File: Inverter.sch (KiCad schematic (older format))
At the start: 96 parts, among them Q1 NTMFS5C670NL, Q2 NTMFS5C670NL, Q3 NTMFS5C670NL, Q4 NTMFS5C670NL, Q5 NTMFS5C670NL, Q6 NTMFS5C670NL, Q7 NTMFS5C670NL, Q8 NTMFS5C670NL, U1 LM5109BMA, U10 NJU77701F, U2 NJU77701F, U3 NJU77701F, U4 LM5109BMA, U5 NJU77701F, U6 NJU77701F, U7 LM5109BMA, U8 NJU77701F, U9 LM5109BMA

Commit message: wip: レグ配線中
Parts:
- added C50, C51, C52, C53: 1uF/50V, Capacitor_SMD:C_0805_2012Metric, symbol Device:C_Small
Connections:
- net GND: now also C50.2, C51.2, C52.2, C53.2
- net VDC: now also C50.1, C51.1, C52.1, C53.1
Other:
- moved on the sheet: C7
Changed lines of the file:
@@
 	4950 3000 4500 3000
 Wire Wire Line
-	4950 3750 4950 3000
-Wire Wire Line
 	4950 4750 4500 4750
-Wire Wire Line
-	4950 3950 4950 4750
 Wire Wire Line
 	4500 4450 4500 4300
@@
 	3050 3500 2900 3500
 $Comp
-L Device:C_Small C7
-U 1 1 606EAE5C
-P 4950 3850
-F 0 "C7" H 5042 3896 50  0000 L CNN
-F 1 "1uF/50V" H 5042 3805 50  0000 L CNN
-F 2 "Capacitor_SMD:C_0805_2012Metric" H 4950 3850 50  0001 C CNN
-F 3 "~" H 4950 3850 50  0001 C CNN
-	1    4950 3850
-	1    0    0    -1
-$EndComp
-$Comp
 L symbols:NTMFS5C670NL Q2
 U 1 1 606EAE62
@@
 $EndComp
 Wire Wire Line
-	8000 3000 7550 3000
-Wire Wire Line
-	8000 3750 8000 3000
-Wire Wire Line
 	7550 4450 7550 4300
 Connection ~ 7550 4450
@@
 $EndComp
 Wire Wire Line
-	11050 3000 10600 3000
-Wire Wire Line
-	11050 3750 11050 3000
-Wire Wire Line
 	10600 4450 10600 4300
 Connection ~ 10600 4450
@@
 	1    0    0    -1
 $EndComp
-Wire Wire Line
-	14100 3000 13650 3000
-Wire Wire Line
-	14100 3750 14100 3000
 Wire Wire Line
 	13650 4450 13650 4300
@@
 Connection ~ 9850 4000
 Connection ~ 6800 4000
+$Comp
+L Device:C_Small C50
+U 1 1 609310E4
+P 5050 3650
+F 0 "C50" H 5142 3696 50  0000 L CNN
+F 1 "1uF/50V" H 5142 3605 50  0000 L CNN
+F 2 "Capacitor_SMD:C_0805_2012Metric" H 5050 3650 50  0001 C CNN
+F 3 "~" H 5050 3650 50  0001 C CNN
+	1    5050 3650
+	1    0    0    -1
+$EndComp
+Wire Wire Line
+	5050 4750 4950 4750
+Wire Wire Line
+	5050 3750 5050 4750
+Connection ~ 4950 4750
+Wire Wire Line
+	5050 3550 5050 3000
+Wire Wire Line
+	5050 3000 4950 3000
+Connection ~ 4950 3000
+Wire Wire Line
+	8100 3550 8100 3000
+$Comp
+L Device:C_Small C51
+U 1 1 609E1815
+P 8100 3650
+F 0 "C51" H 8192 3696 50  0000 L CNN
+F 1 "1uF/50V" H 8192 3605 50  0000 L CNN
+F 2 "Capacitor_SMD:C_0805_2012Metric" H 8100 3650 50  0001 C CNN
+F 3 "~" H 8100 3650 50  0001 C CNN
+	1    8100 3650
+	1    0    0    -1
+$EndComp
+Wire Wire Line
+	8100 3750 8100 4750
+Wire Wire Line
+	8000 3000 7550 3000
+Wire Wire Line
+	8000 3750 8000 3000
+Wire Wire Line
+	8100 3000 8000 3000
+Connection ~ 8000 3000
 Wire Wire Line
 	7550 4750 8000 4750
@@
 	8000 3950 8000 4750
 Wire Wire Line
+	8100 4750 8000 4750
+Connection ~ 8000 4750
+Wire Wire Line
+	11150 3550 11150 3000
+$Comp
+L Device:C_Small C52
+U 1 1 60ABFB83
+P 11150 3650
+F 0 "C52" H 11242 3696 50  0000 L CNN
+F 1 "1uF/50V" H 11242 3605 50  0000 L CNN
+F 2 "Capacitor_SMD:C_0805_2012Metric" H 11150 3650 50  0001 C CNN
+F 3 "~" H 11150 3650 50  0001 C CNN
+	1    11150 3650
+	1    0    0    -1
+$EndComp
+Wire Wire Line
+	11150 3750 11150 4750
+Wire Wire Line
+	11050 3000 10600 3000
+Wire Wire Line
+	11050 3750 11050 3000
+Wire Wire Line
+	11150 3000 11050 3000
+Connection ~ 11050 3000
+Wire Wire Line
 	11050 4750 10600 4750
 Wire Wire Line
 	11050 3950 11050 4750
 Wire Wire Line
+	11150 4750 11050 4750
+Connection ~ 11050 4750
+Wire Wire Line
+	14200 3550 14200 3000
+$Comp
+L Device:C_Small C53
+U 1 1 60BA2636
+P 14200 3650
+F 0 "C53" H 14292 3696 50  0000 L CNN
+F 1 "1uF/50V" H 14292 3605 50  0000 L CNN
+F 2 "Capacitor_SMD:C_0805_2012Metric" H 14200 3650 50  0001 C CNN
+F 3 "~" H 14200 3650 50  0001 C CNN
+	1    14200 3650
+	1    0    0    -1
+$EndComp
+Wire Wire Line
+	14200 3750 14200 4750
+Wire Wire Line
+	14100 3000 13650 3000
+Wire Wire Line
+	14100 3750 14100 3000
+Wire Wire Line
+	14200 3000 14100 3000
+Connection ~ 14100 3000
+Wire Wire Line
 	14100 4750 13650 4750
 Wire Wire Line
 	14100 3950 14100 4750
+Wire Wire Line
+	14200 4750 14100 4750
+Connection ~ 14100 4750
+$Comp
+L Device:C_Small C7
+U 1 1 606EAE5C
+P 4950 3900
+F 0 "C7" H 5042 3946 50  0000 L CNN
+F 1 "1uF/50V" H 5042 3855 50  0000 L CNN
+F 2 "Capacitor_SMD:C_0805_2012Metric" H 4950 3900 50  0001 C CNN
+F 3 "~" H 4950 3900 50  0001 C CNN
+	1    4950 3900
+	1    0    0    -1
+$EndComp
+Wire Wire Line
+	4950 3800 4950 3000
+Wire Wire Line
+	4950 4000 4950 4750
 Wire Bus Line
 	11550 4000 11550 7450

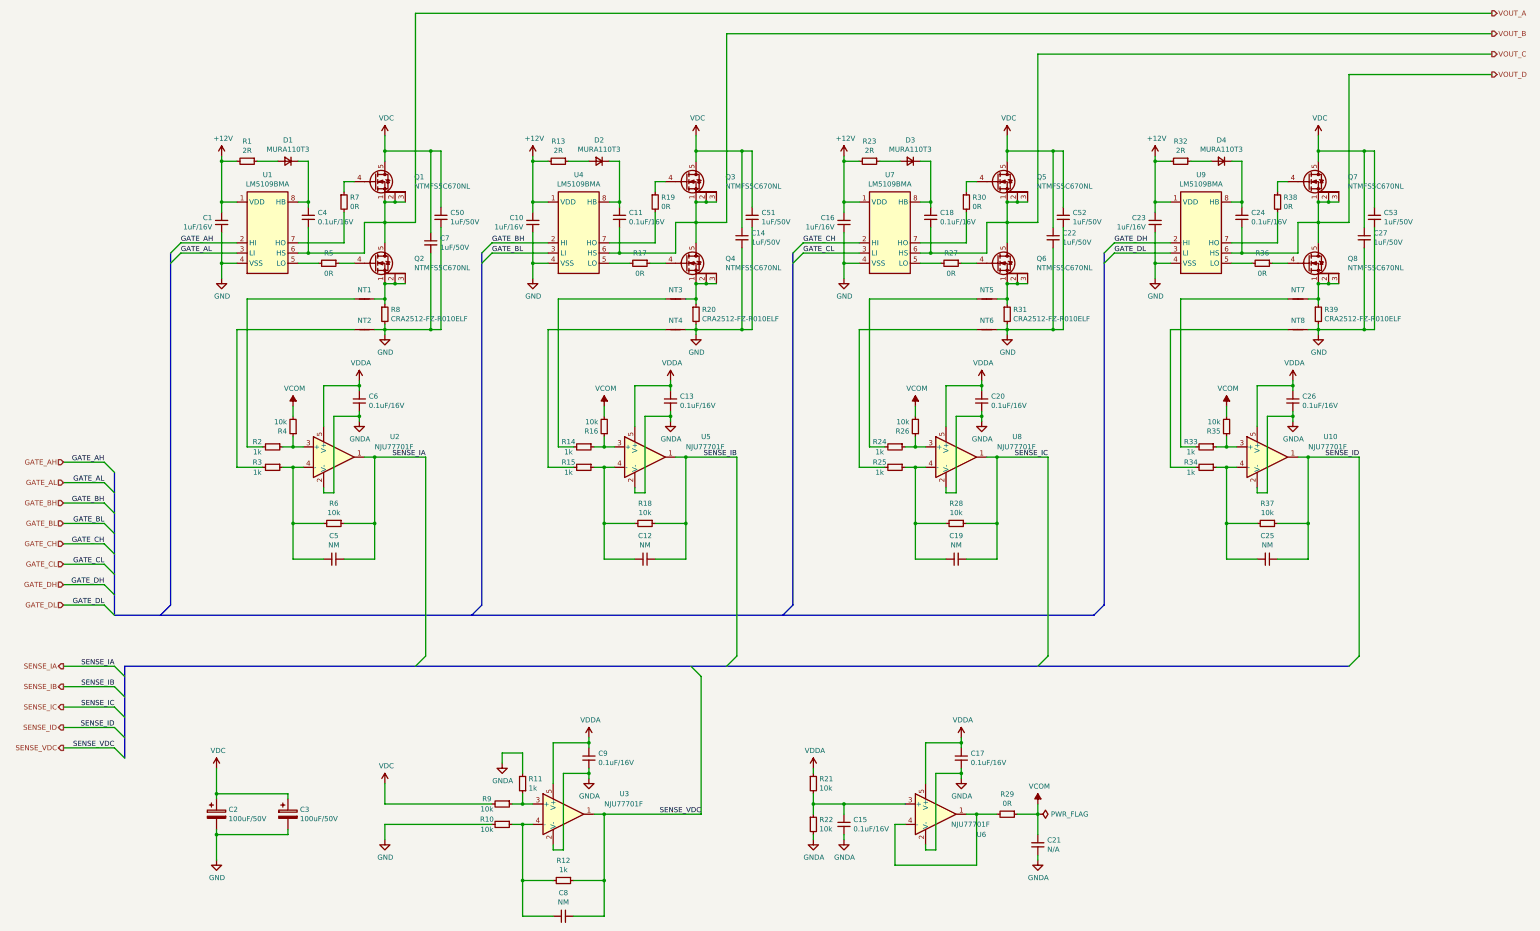
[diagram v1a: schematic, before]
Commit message: Update: 回路図、DCリンクCap1つ削除、アノテーションリセット
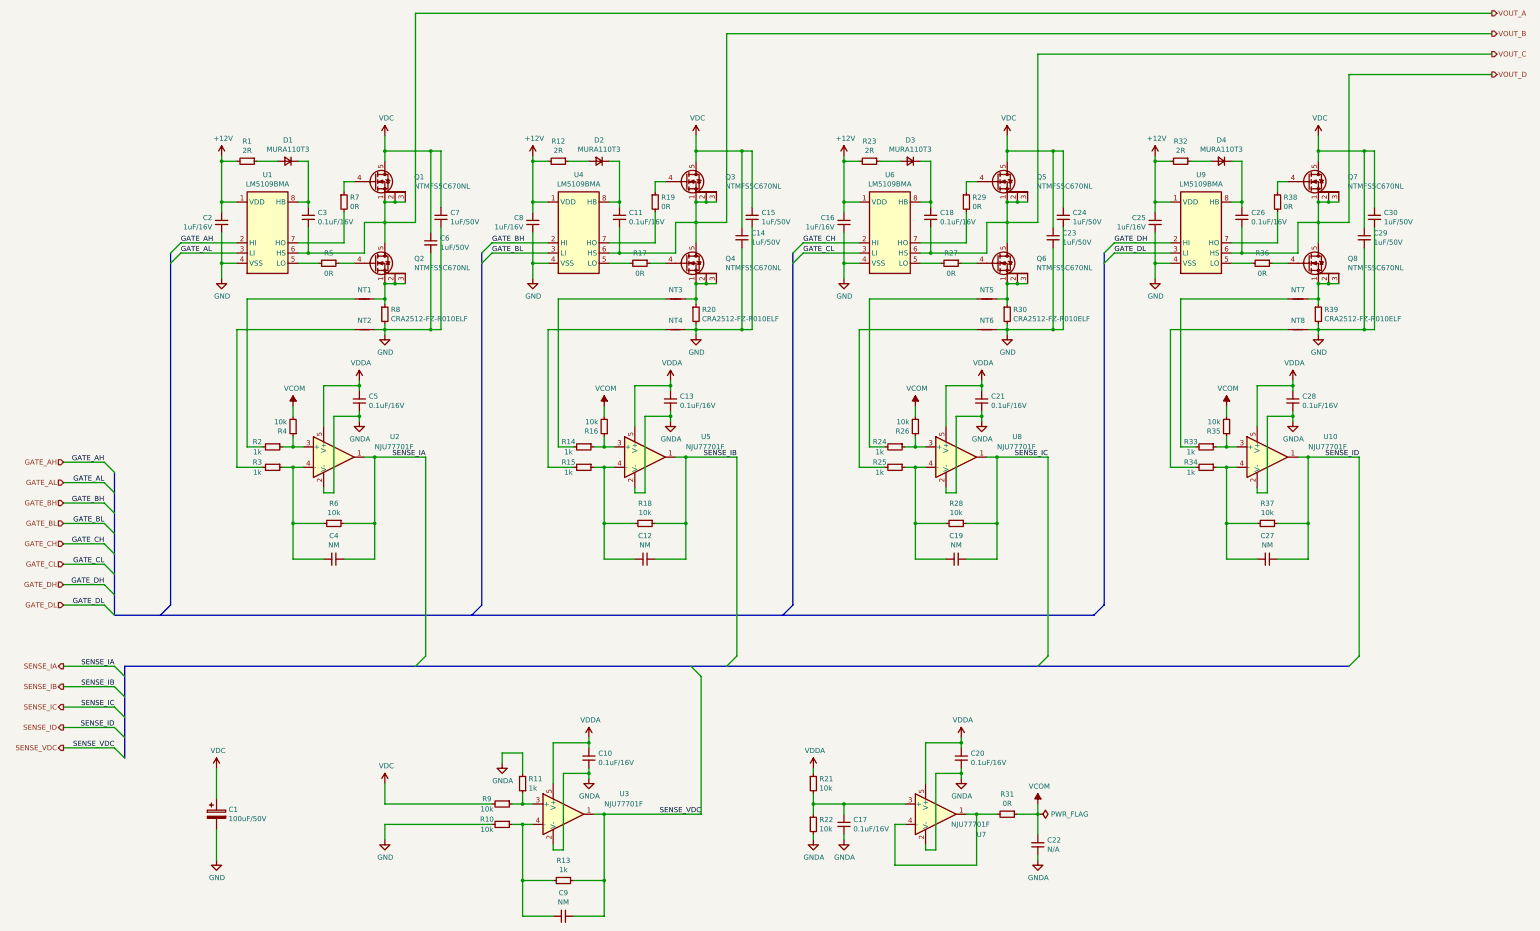
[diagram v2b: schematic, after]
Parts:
- removed C3: 100uF/50V, Capacitor_SMD:CP_Elec_10x10, symbol Device:CP
- renumbered C2 to C1, C9 to C10, C51 to C15, C15 to C17, C1 to C2, C17 to C20, C20 to C21, C21 to C22, C22 to C23, C52 to C24, C23 to C25, C24 to C26, C25 to C27, C26 to C28, C27 to C29, C4 to C3, C53 to C30, C5 to C4, C6 to C5, C7 to C6, C50 to C7, C10 to C8, C8 to C9, R13 to R12, R12 to R13, R30 to R29, R31 to R30, R29 to R31, U7 to U6, U6 to U7

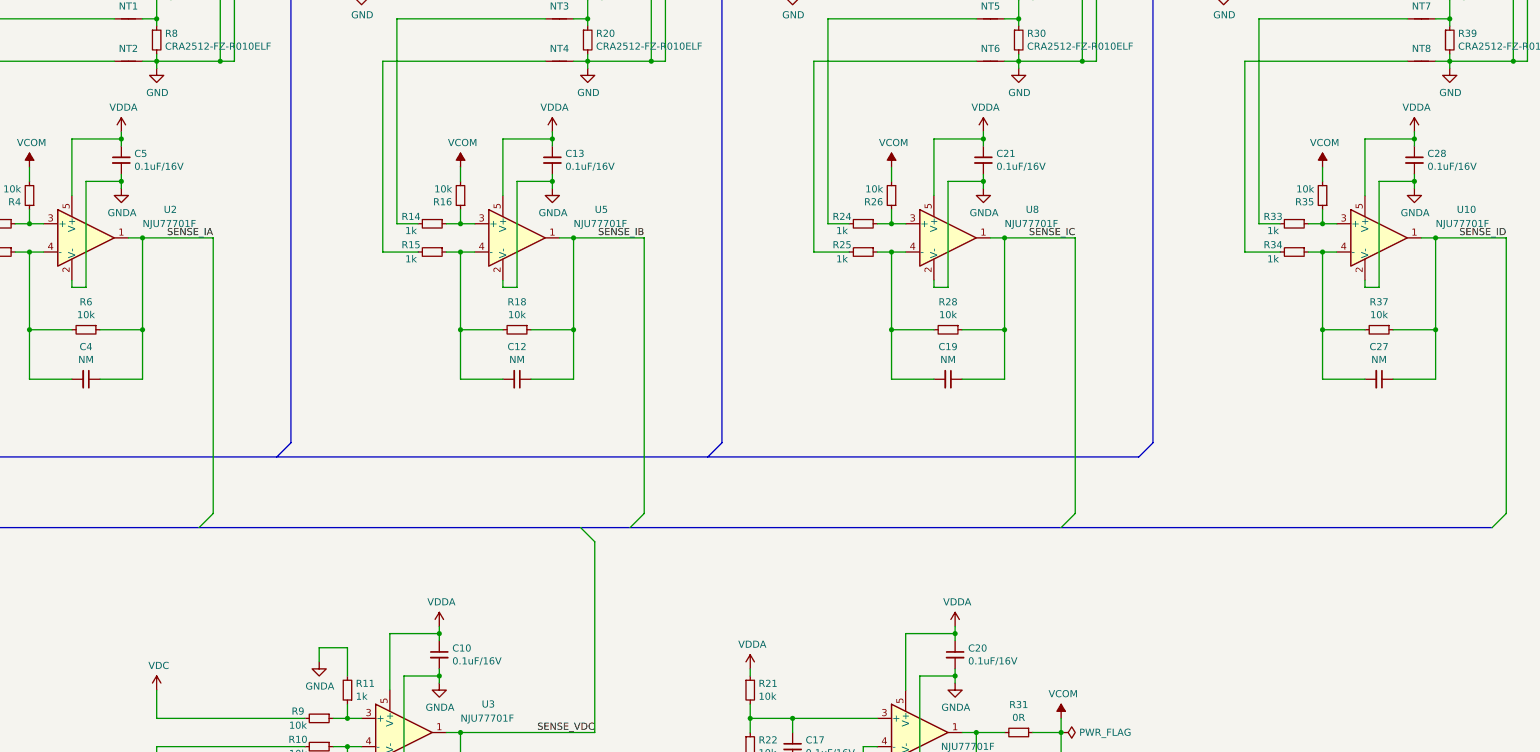
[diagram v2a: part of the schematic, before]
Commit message: Update: アナログリファレンスをLDOからに変更
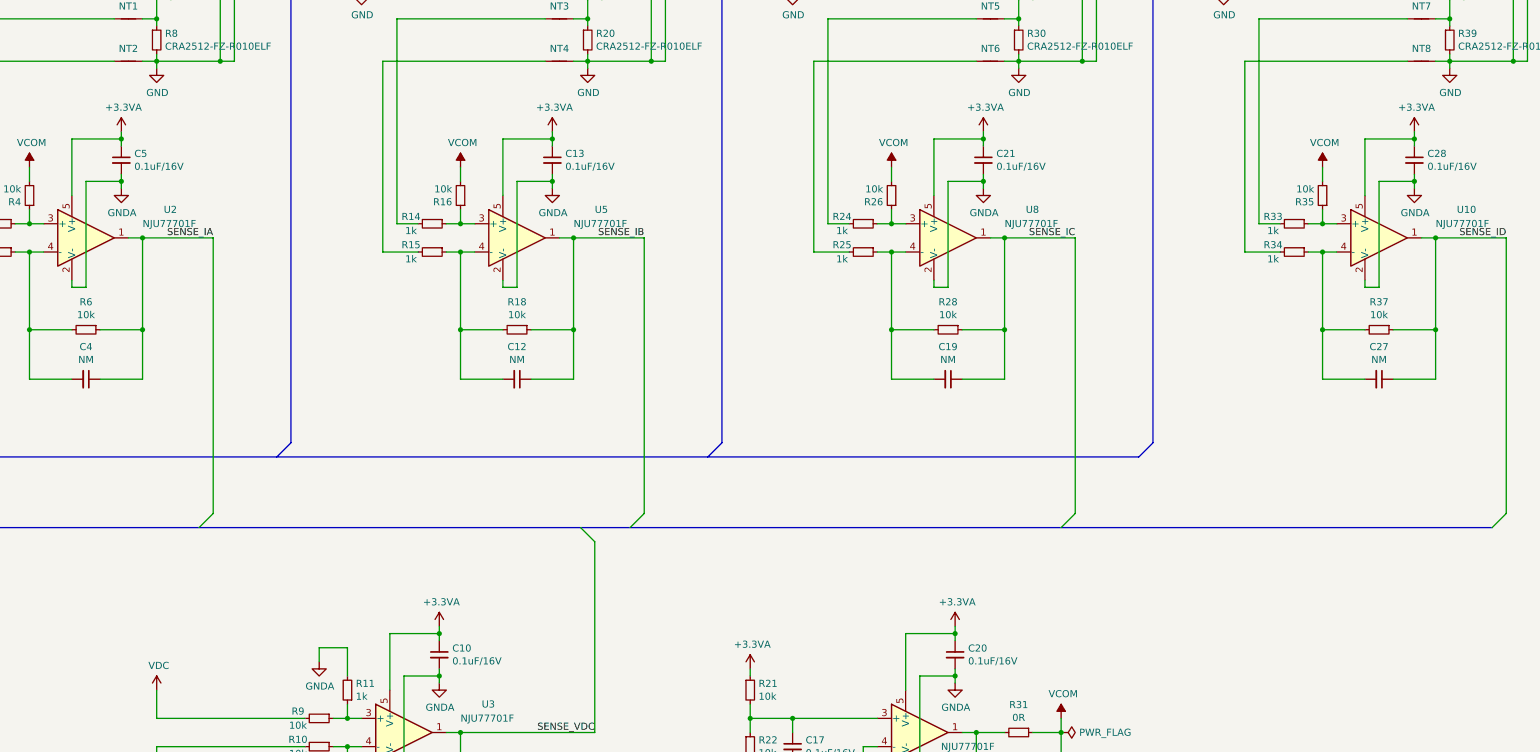
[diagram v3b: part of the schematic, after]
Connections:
- net VDDA renamed +3.3VA
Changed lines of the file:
@@
 	4250 5300 3900 5300
-$Comp
-L power:VDDA #PWR018
-U 1 1 606EAC97
-P 4250 5250
-F 0 "#PWR018" H 4250 5100 50  0001 C CNN
-F 1 "VDDA" H 4265 5423 50  0000 C CNN
-F 2 "" H 4250 5250 50  0001 C CNN
-F 3 "" H 4250 5250 50  0001 C CNN
-	1    4250 5250
-	1    0    0    -1
-$EndComp
 $Comp
 L Device:C_Small C5
@@
 	7300 5300 6950 5300
 $Comp
-L power:VDDA #PWR030
-U 1 1 606EACF8
-P 7300 5250
-F 0 "#PWR030" H 7300 5100 50  0001 C CNN
-F 1 "VDDA" H 7315 5423 50  0000 C CNN
-F 2 "" H 7300 5250 50  0001 C CNN
-F 3 "" H 7300 5250 50  0001 C CNN
-	1    7300 5250
-	1    0    0    -1
-$EndComp
-$Comp
 L Device:C_Small C13
 U 1 1 606EACFE
@@
 	10350 5300 10000 5300
 $Comp
-L power:VDDA #PWR042
-U 1 1 606EAD59
-P 10350 5250
-F 0 "#PWR042" H 10350 5100 50  0001 C CNN
-F 1 "VDDA" H 10365 5423 50  0000 C CNN
-F 2 "" H 10350 5250 50  0001 C CNN
-F 3 "" H 10350 5250 50  0001 C CNN
-	1    10350 5250
-	1    0    0    -1
-$EndComp
-$Comp
 L Device:C_Small C21
 U 1 1 606EAD5F
@@
 Wire Wire Line
 	13400 5300 13050 5300
-$Comp
-L power:VDDA #PWR051
-U 1 1 606EADBA
-P 13400 5250
-F 0 "#PWR051" H 13400 5100 50  0001 C CNN
-F 1 "VDDA" H 13415 5423 50  0000 C CNN
-F 2 "" H 13400 5250 50  0001 C CNN
-F 3 "" H 13400 5250 50  0001 C CNN
-	1    13400 5250
-	1    0    0    -1
-$EndComp
 $Comp
 L Device:C_Small C28
@@
 F 3 "~" H 6500 8950 50  0001 C CNN
 	1    6500 8950
-	1    0    0    -1
-$EndComp
-$Comp
-L power:VDDA #PWR?
-U 1 1 60A370A3
-P 6500 8750
-AR Path="/60A370A3" Ref="#PWR?"  Part="1"
-AR Path="/6062D296/60A370A3" Ref="#PWR027"  Part="1"
-F 0 "#PWR027" H 6500 8600 50  0001 C CNN
-F 1 "VDDA" H 6515 8923 50  0000 C CNN
-F 2 "" H 6500 8750 50  0001 C CNN
-F 3 "" H 6500 8750 50  0001 C CNN
-	1    6500 8750
 	1    0    0    -1
 $EndComp
@@
 Wire Wire Line
 	8700 9300 8700 9400
-$Comp
-L power:VDDA #PWR?
-U 1 1 61C3D321
-P 8700 9050
-AR Path="/61C3D321" Ref="#PWR?"  Part="1"
-AR Path="/6093BF63/61C3D321" Ref="#PWR?"  Part="1"
-AR Path="/6062D296/61C3D321" Ref="#PWR034"  Part="1"
-F 0 "#PWR034" H 8700 8900 50  0001 C CNN
-F 1 "VDDA" H 8715 9223 50  0000 C CNN
-F 2 "" H 8700 9050 50  0001 C CNN
-F 3 "" H 8700 9050 50  0001 C CNN
-	1    8700 9050
-	1    0    0    -1
-$EndComp
 Wire Wire Line
 	8700 9050 8700 9100
@@
 F 3 "" H 10150 9150 50  0001 C CNN
 	1    10150 9150
-	1    0    0    -1
-$EndComp
-$Comp
-L power:VDDA #PWR?
-U 1 1 61C3D368
-P 10150 8750
-AR Path="/61C3D368" Ref="#PWR?"  Part="1"
-AR Path="/6093BF63/61C3D368" Ref="#PWR?"  Part="1"
-AR Path="/6062D296/61C3D368" Ref="#PWR040"  Part="1"
-F 0 "#PWR040" H 10150 8600 50  0001 C CNN
-F 1 "VDDA" H 10165 8923 50  0000 C CNN
-F 2 "" H 10150 8750 50  0001 C CNN
-F 3 "" H 10150 8750 50  0001 C CNN
-	1    10150 8750
 	1    0    0    -1
 $EndComp
@@
 Wire Wire Line
 	2850 9650 2850 9950
+$Comp
+L power:+3.3VA #PWR?
+U 1 1 607D37CC
+P 13400 5250
+AR Path="/607D8C01/607D37CC" Ref="#PWR?"  Part="1"
+AR Path="/6062D296/607D37CC" Ref="#PWR051"  Part="1"
+F 0 "#PWR051" H 13400 5100 50  0001 C CNN
+F 1 "+3.3VA" H 13415 5423 50  0000 C CNN
+F 2 "" H 13400 5250 50  0001 C CNN
+F 3 "" H 13400 5250 50  0001 C CNN
+	1    13400 5250
+	1    0    0    -1
+$EndComp
+$Comp
+L power:+3.3VA #PWR?
+U 1 1 6082C7D4
+P 10350 5250
+AR Path="/607D8C01/6082C7D4" Ref="#PWR?"  Part="1"
+AR Path="/6062D296/6082C7D4" Ref="#PWR042"  Part="1"
+F 0 "#PWR042" H 10350 5100 50  0001 C CNN
+F 1 "+3.3VA" H 10365 5423 50  0000 C CNN
+F 2 "" H 10350 5250 50  0001 C CNN
+F 3 "" H 10350 5250 50  0001 C CNN
+	1    10350 5250
+	1    0    0    -1
+$EndComp
+$Comp
+L power:+3.3VA #PWR?
+U 1 1 60858FA0
+P 7300 5250
+AR Path="/607D8C01/60858FA0" Ref="#PWR?"  Part="1"
+AR Path="/6062D296/60858FA0" Ref="#PWR030"  Part="1"
+F 0 "#PWR030" H 7300 5100 50  0001 C CNN
+F 1 "+3.3VA" H 7315 5423 50  0000 C CNN
+F 2 "" H 7300 5250 50  0001 C CNN
+F 3 "" H 7300 5250 50  0001 C CNN
+	1    7300 5250
+	1    0    0    -1
+$EndComp
+$Comp
+L power:+3.3VA #PWR?
+U 1 1 60885659
+P 4250 5250
+AR Path="/607D8C01/60885659" Ref="#PWR?"  Part="1"
+AR Path="/6062D296/60885659" Ref="#PWR018"  Part="1"
+F 0 "#PWR018" H 4250 5100 50  0001 C CNN
+F 1 "+3.3VA" H 4265 5423 50  0000 C CNN
+F 2 "" H 4250 5250 50  0001 C CNN
+F 3 "" H 4250 5250 50  0001 C CNN
+	1    4250 5250
+	1    0    0    -1
+$EndComp
+$Comp
+L power:+3.3VA #PWR?
+U 1 1 608DED1F
+P 10150 8750
+AR Path="/607D8C01/608DED1F" Ref="#PWR?"  Part="1"
+AR Path="/6062D296/608DED1F" Ref="#PWR040"  Part="1"
+F 0 "#PWR040" H 10150 8600 50  0001 C CNN
+F 1 "+3.3VA" H 10165 8923 50  0000 C CNN
+F 2 "" H 10150 8750 50  0001 C CNN
+F 3 "" H 10150 8750 50  0001 C CNN
+	1    10150 8750
+	1    0    0    -1
+$EndComp
+$Comp
+L power:+3.3VA #PWR?
+U 1 1 60939200
+P 8700 9050
+AR Path="/607D8C01/60939200" Ref="#PWR?"  Part="1"
+AR Path="/6062D296/60939200" Ref="#PWR034"  Part="1"
+F 0 "#PWR034" H 8700 8900 50  0001 C CNN
+F 1 "+3.3VA" H 8715 9223 50  0000 C CNN
+F 2 "" H 8700 9050 50  0001 C CNN
+F 3 "" H 8700 9050 50  0001 C CNN
+	1    8700 9050
+	1    0    0    -1
+$EndComp
+$Comp
+L power:+3.3VA #PWR?
+U 1 1 60992885
+P 6500 8750
+AR Path="/607D8C01/60992885" Ref="#PWR?"  Part="1"
+AR Path="/6062D296/60992885" Ref="#PWR027"  Part="1"
+F 0 "#PWR027" H 6500 8600 50  0001 C CNN
+F 1 "+3.3VA" H 6515 8923 50  0000 C CNN
+F 2 "" H 6500 8750 50  0001 C CNN
+F 3 "" H 6500 8750 50  0001 C CNN
+	1    6500 8750
+	1    0    0    -1
+$EndComp
 Wire Bus Line
 	11550 4000 11550 7450
@@
 	2400 4000 2400 7450
 Wire Bus Line
+	1950 8050 1950 8950
+Wire Bus Line
 	1850 7550 11450 7550
 Wire Bus Line
-	1950 8050 1950 8950
-Wire Bus Line
 	1950 8050 13950 8050
